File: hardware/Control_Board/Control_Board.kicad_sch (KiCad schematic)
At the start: 5 parts, among them J1 Left Motor, J2 Right Motor, J3 ICSP Socket, U1 APC220, U2 PIC16F1705

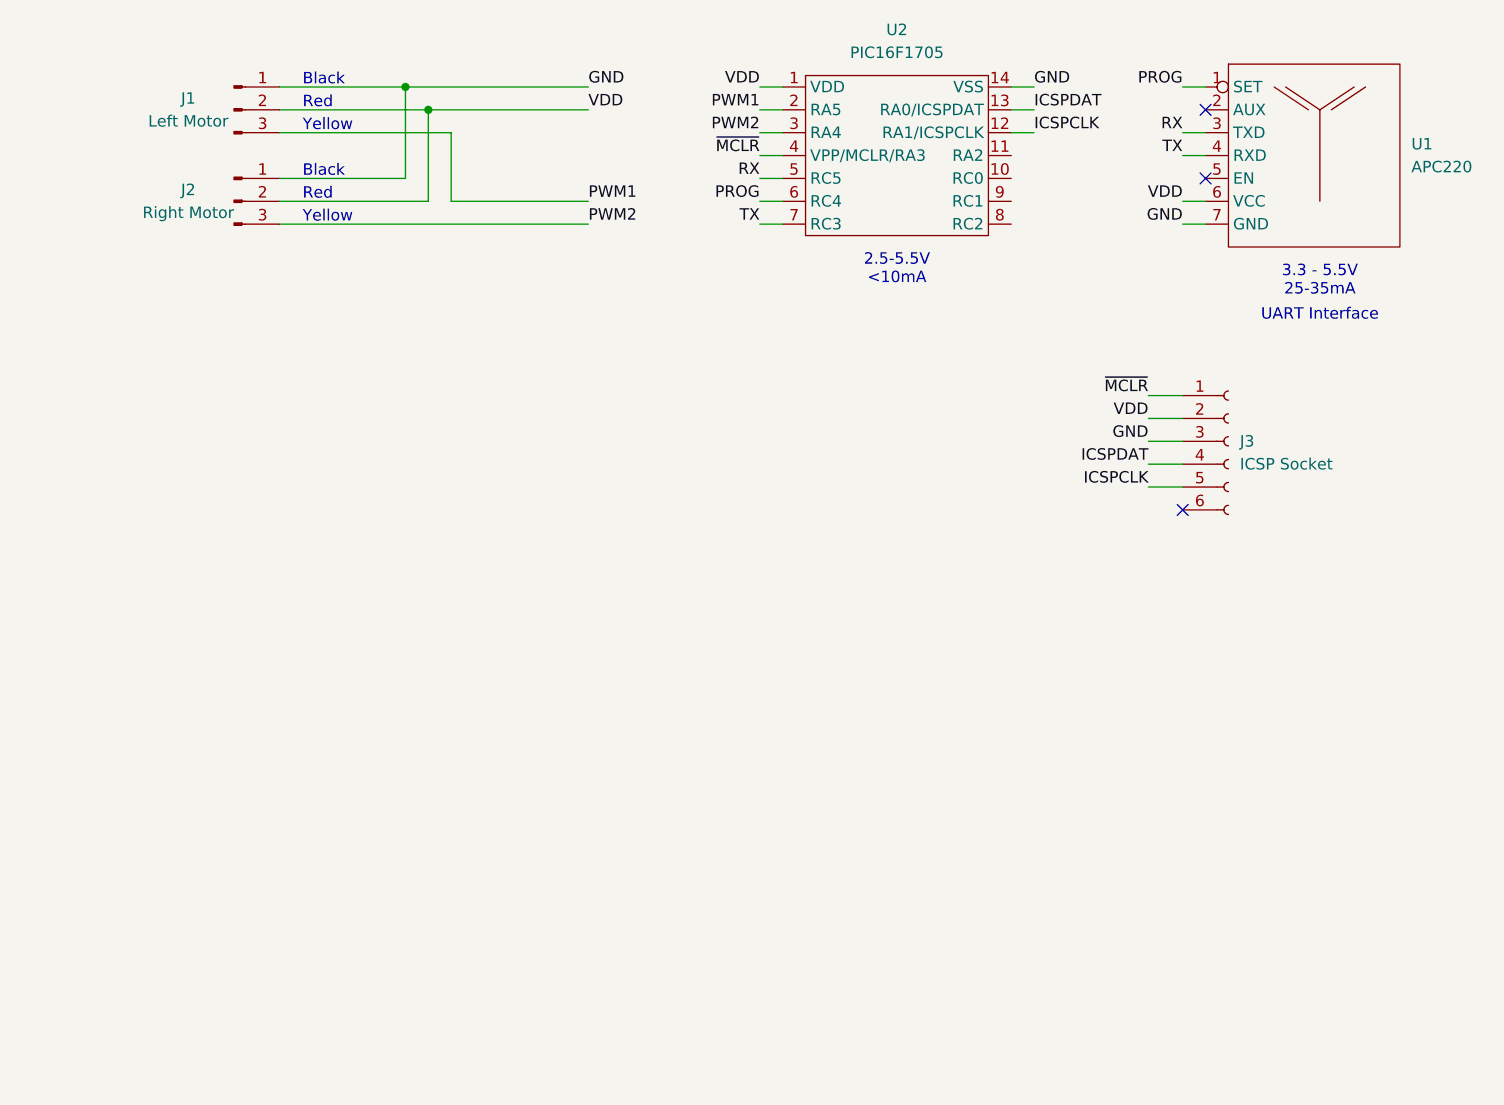
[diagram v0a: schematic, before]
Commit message: feat: create initial test board
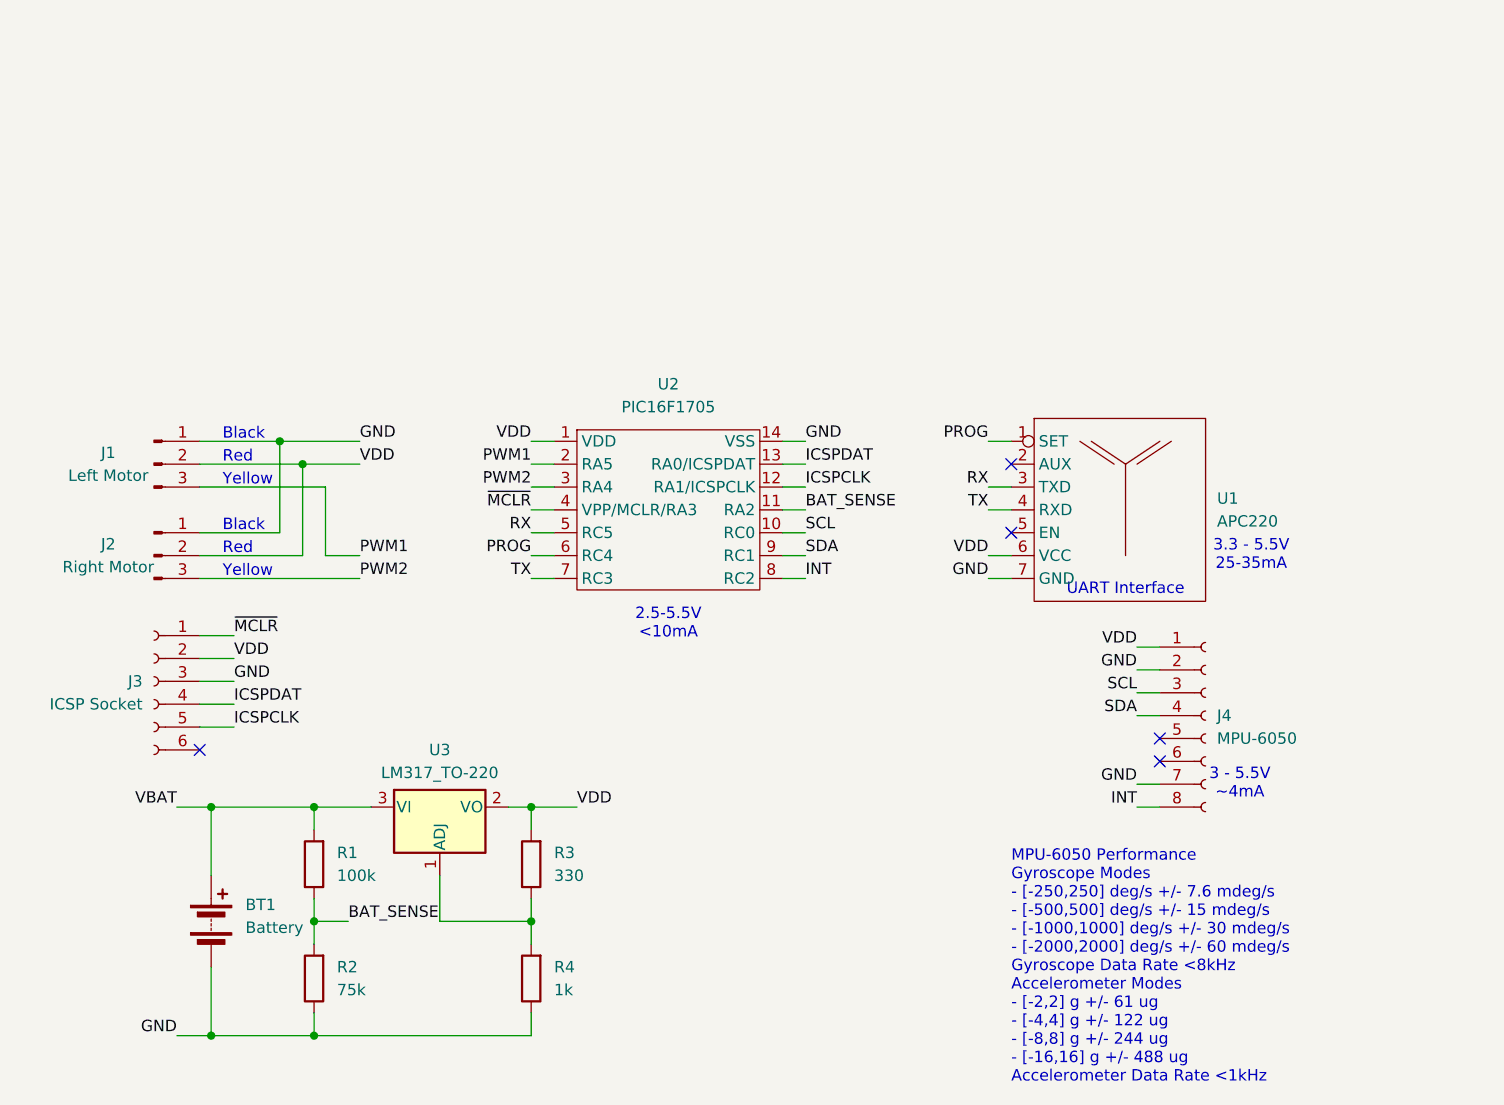
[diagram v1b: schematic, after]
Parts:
- added BT1: Battery, symbol Device:Battery
- added J4: MPU-6050, symbol Connector:Conn_01x08_Socket
- added R1: 100k, symbol Device:R
- added R2: 75k, symbol Device:R
- added R3: 330, symbol Device:R
- added R4: 1k, symbol Device:R
- added U3: LM317_TO-220, Package_TO_SOT_THT:TO-220-3_Vertical, symbol Regulator_Linear:LM317_TO-220
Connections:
- net GND: now also BT1.2 (-), J4.2 (Pin_2), J4.7 (Pin_7), R2.1, R4.1
- net VDD: now also J4.1 (Pin_1), R3.2, U3.2 (VO)
- net SCL: now reaches U2.10 (RC0)
- net SCL: now also J4.3 (Pin_3)
- net BAT_SENSE: now reaches U2.11 (RA2)
- net BAT_SENSE: now also R1.1, R2.2
- net INT: now reaches U2.8 (RC2)
- net INT: now also J4.8 (Pin_8)
- net SDA: now reaches U2.9 (RC1)
- net SDA: now also J4.4 (Pin_4)
- new net: R3.1, R4.2, U3.1 (ADJ)
- new net VBAT: BT1.1 (+), R1.2, U3.3 (VI)
- no-connect marks 3 -> 5
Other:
- note added: "3 - 5.5V ~4mA"
- note added: "MPU-6050 Performance Gyroscope Modes - [-250,250] deg/s +/- 7.6 mdeg/s - [-500,500] deg/s +/- 15 mdeg/s - [-1000,1000] deg/s +/- 30 mdeg/s - [-2000,2000] deg/s +/- 60 mdeg/s Gyroscope Data Rate <8kHz Accelerometer Modes - [-2,2] g +/- 61 ug - [-4,4] g +/- 122 ug - [-8,8] g +/- 244 ug - [-16,16] g +/- 488 ug Accelerometer Data Rate <1kHz"
- moved on the sheet: J1, J2, J3, U1, U2

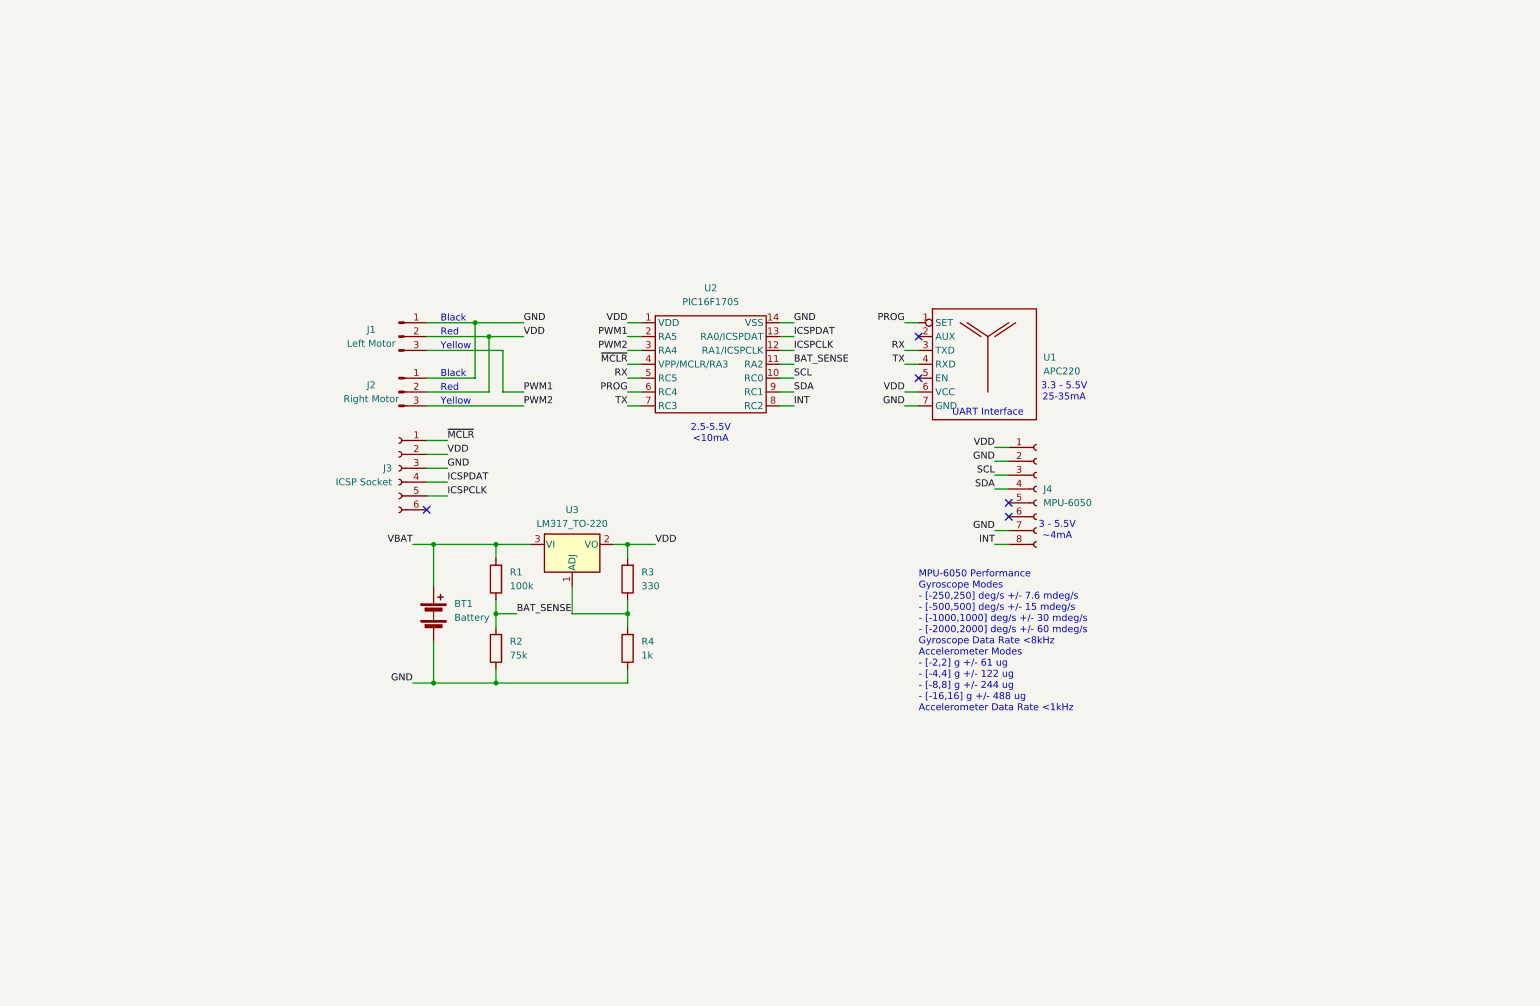
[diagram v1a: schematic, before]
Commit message: feat: update prototype with esp32
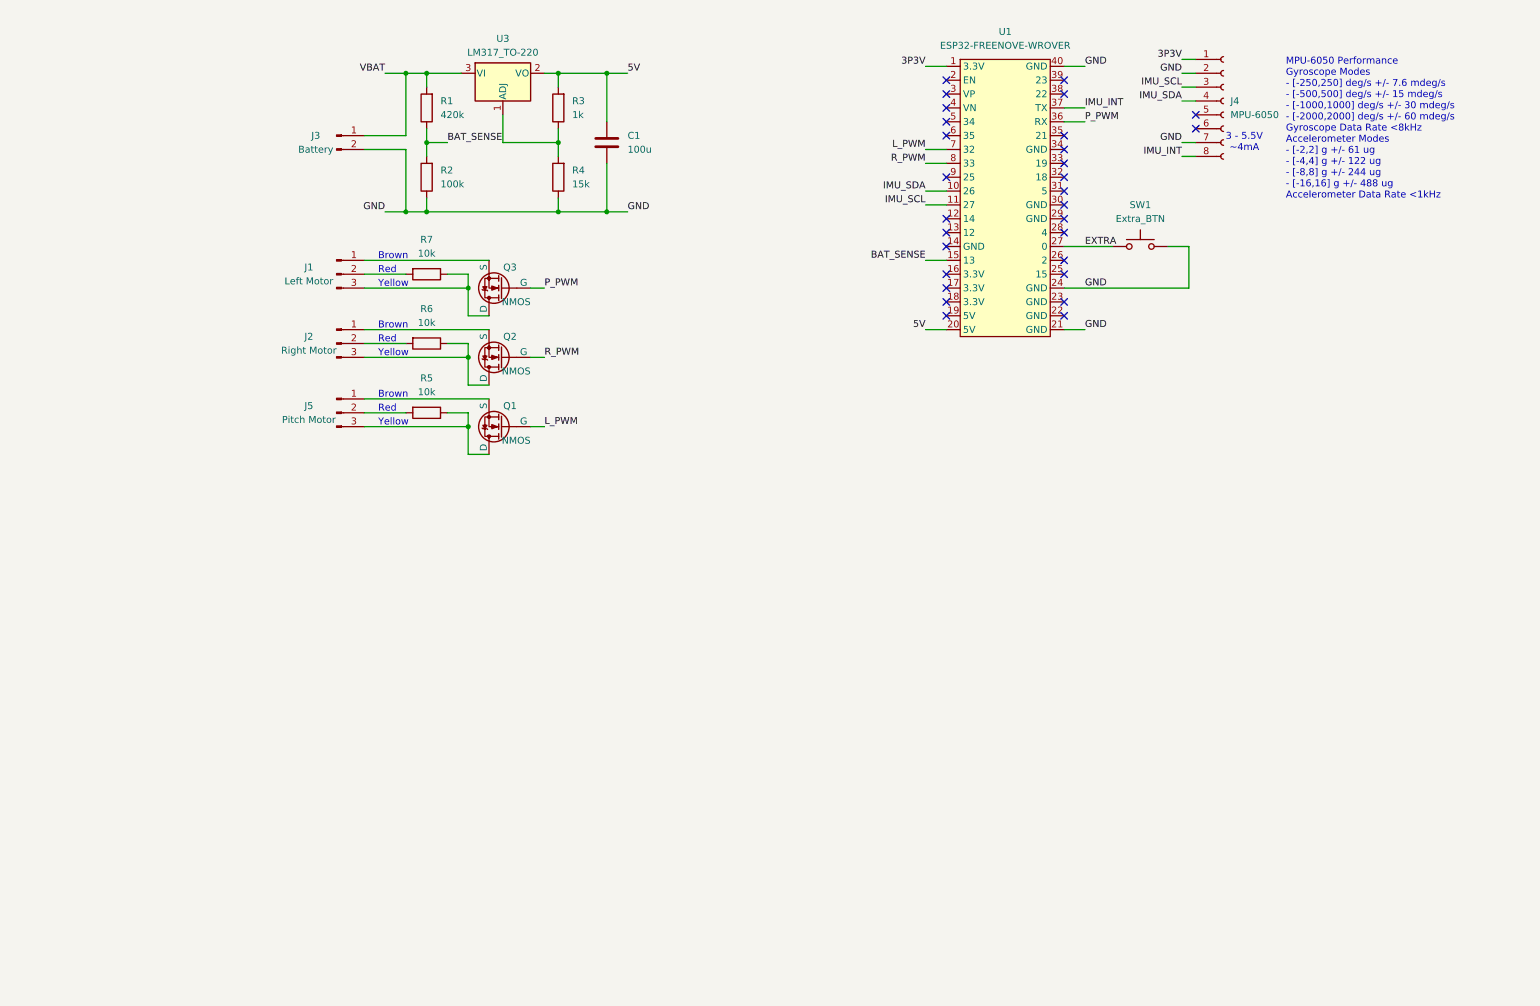
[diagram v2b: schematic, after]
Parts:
- removed BT1: Battery, symbol Device:Battery
- removed J3: ICSP Socket, symbol Connector:Conn_01x06_Socket
- removed U1: APC220, symbol APC220:APC220
- removed U2: PIC16F1705, Package_DIP:DIP-14_W7.62mm, symbol PIC16F1705:PIC16F1705
- added C1: 100u, Capacitor_THT:C_Disc_D3.0mm_W1.6mm_P2.50mm, symbol Device:C
- added J3: Battery, Connector_PinHeader_2.54mm:PinHeader_1x02_P2.54mm_Vertical, symbol Connector:Conn_01x02_Pin
- added J5: Pitch Motor, Connector_PinHeader_2.54mm:PinHeader_1x03_P2.54mm_Vertical, symbol Connector:Conn_01x03_Pin
- added Q1, Q2, Q3: NMOS, Connector_PinHeader_2.54mm:PinHeader_1x03_P2.54mm_Vertical, symbol Simulation_SPICE:NMOS
- added R5, R6, R7: 10k, Resistor_THT:R_Axial_DIN0207_L6.3mm_D2.5mm_P10.16mm_Horizontal, symbol Device:R
- added SW1: Extra_BTN, symbol Switch:SW_Push
- added U1: ESP32-FREENOVE-WROVER, PCM_Espressif:ESP32-FREENOVE-WROVER, symbol PCM_Espressif:ESP32-FREENOVE-WROVER
- J1, J2: footprint (none) -> Connector_PinHeader_2.54mm:PinHeader_1x03_P2.54mm_Vertical
- J4: footprint (none) -> Connector_PinSocket_2.54mm:PinSocket_1x08_P2.54mm_Vertical
- R1: value 100k -> 420k; footprint (none) -> Resistor_THT:R_Axial_DIN0207_L6.3mm_D2.5mm_P10.16mm_Horizontal
- R2: value 75k -> 100k; footprint (none) -> Resistor_THT:R_Axial_DIN0207_L6.3mm_D2.5mm_P10.16mm_Horizontal
- R3: value 330 -> 1k; footprint (none) -> Resistor_THT:R_Axial_DIN0207_L6.3mm_D2.5mm_P10.16mm_Horizontal
- R4: value 1k -> 15k; footprint (none) -> Resistor_THT:R_Axial_DIN0207_L6.3mm_D2.5mm_P10.16mm_Horizontal
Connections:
- net BAT_SENSE: now also U1.15 (13)
- net GND: now also C1.2, J3.2 (Pin_2), SW1.2, U1.21 (GND), U1.24 (GND), U1.40 (GND); no longer J1.1 (Pin_1), J2.1 (Pin_1)
- net VBAT: now also J3.1 (Pin_1)
- net INT renamed IMU_INT
- net IMU_INT: now also U1.37 (TX)
- net PWM1: no longer names the net of J1.3 (Pin_3)
- net PWM1: now also Q3.1 (D), R7.1
- net PWM2: no longer names the net of J2.3 (Pin_3)
- net PWM2: now also Q2.1 (D), R6.1
- net SCL renamed IMU_SCL
- net IMU_SCL: now also U1.11 (27)
- net SDA renamed IMU_SDA
- net IMU_SDA: now also U1.10 (26)
- removed net VDD: J1.2 (Pin_2), J2.2 (Pin_2), J4.1 (Pin_1), R3.2, U3.2 (VO)
- new net: J5.3 (Pin_3), Q1.1 (D), R5.1
- new net: J5.2 (Pin_2), R5.2
- new net: J2.1 (Pin_1), Q2.3 (S)
- new net: J1.2 (Pin_2), R7.2
- new net: J1.1 (Pin_1), Q3.3 (S)
- new net: J5.1 (Pin_1), Q1.3 (S)
- new net: J2.2 (Pin_2), R6.2
- new net 3P3V: J4.1 (Pin_1), U1.1 (3.3V)
- new net 5V: C1.1, R3.2, U1.20 (5V), U3.2 (VO)
- new net EXTRA: SW1.1, U1.27 (0)
- new net L_PWM: Q1.2 (G), U1.7 (32)
- new net P_PWM: Q3.2 (G), U1.36 (RX)
- new net R_PWM: Q2.2 (G), U1.8 (33)
- no-connect marks 5 -> 29
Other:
- note added: "Brown"
- note removed: "2.5-5.5V <10mA"
- note removed: "3.3 - 5.5V 25-35mA"
- note removed: "Black"
- note removed: "UART Interface"
- moved on the sheet: J1, J2, J4, R1, R2, R3, R4, U3

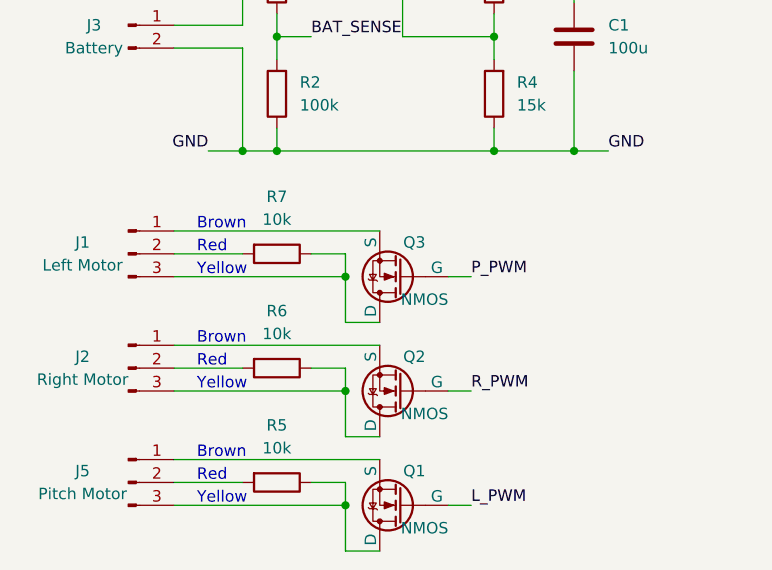
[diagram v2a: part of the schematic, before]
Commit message: feat: update and reorganize MPU Code
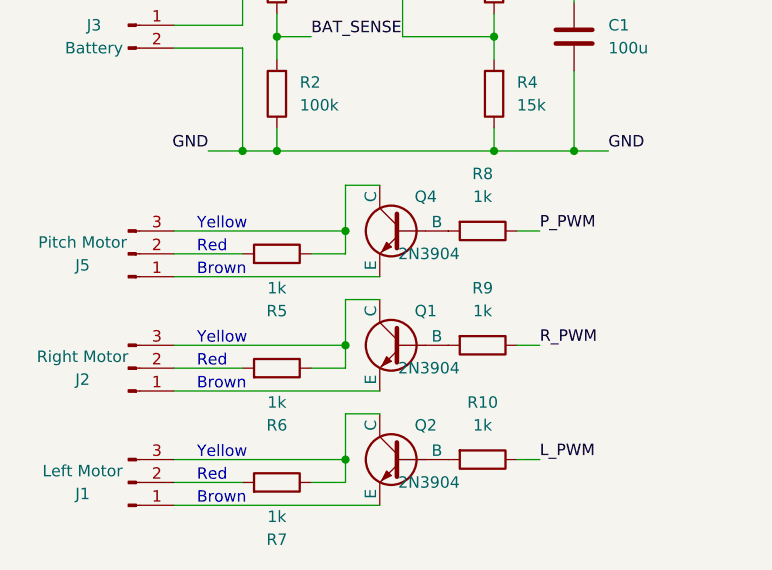
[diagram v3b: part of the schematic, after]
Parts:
- removed Q1, Q2, Q3: NMOS, Connector_PinHeader_2.54mm:PinHeader_1x03_P2.54mm_Vertical, symbol Simulation_SPICE:NMOS
- added Q1, Q2, Q4: 2N3904, Package_TO_SOT_THT:TO-92_Inline, symbol Simulation_SPICE:NPN
- added R10, R8, R9: 1k, Resistor_THT:R_Axial_DIN0207_L6.3mm_D2.5mm_P10.16mm_Horizontal, symbol Device:R
- R5, R6, R7: value 10k -> 1k
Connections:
- net L_PWM: now also R10.1
- net P_PWM: now also R8.1
- net R_PWM: now also R9.1
- net at J5.3 (Pin_3), R5.1: now also Q4.1 (C)
- net at J2.3 (Pin_3), R6.1: now also Q1.1 (C)
- net at J2.1 (Pin_1): now also Q1.3 (E)
- net at J1.3 (Pin_3), R7.1: now also Q2.1 (C)
- net at J1.1 (Pin_1): now also Q2.3 (E)
- net at J5.1 (Pin_1): now also Q4.3 (E)
- new net: Q2.2 (B), R10.2
- new net: Q4.2 (B), R8.2
- new net: Q1.2 (B), R9.2
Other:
- moved on the sheet: J1, J5, R5, R7
